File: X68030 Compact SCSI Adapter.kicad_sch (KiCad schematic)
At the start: 2 parts, among them J1 X68030 Internal SCSI Connector, J2 DB25_Plug_MountingHoles

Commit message: Rev 2.0
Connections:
- net ATN: now also J1.35 (Pin_35); no longer J1.32 (Pin_32)
- net CD: now also J1.44 (Pin_44); no longer J1.46 (Pin_46)
- net DB0: now also J1.16 (Pin_16); no longer J1.2 (Pin_2)
- net DB1: now also J1.18 (Pin_18); no longer J1.4 (Pin_4)
- net DB2: now also J1.20 (Pin_20); no longer J1.6 (Pin_6)
- net DB3: now also J1.22 (Pin_22); no longer J1.8 (Pin_8)
- net DB4: now also J1.24 (Pin_24); no longer J1.10 (Pin_10)
- net DB5: now also J1.26 (Pin_26); no longer J1.12 (Pin_12)
- net DB6: now also J1.28 (Pin_28); no longer J1.14 (Pin_14)
- net DB7: now also J1.30 (Pin_30); no longer J1.16 (Pin_16)
- net DBP: now also J1.32 (Pin_32); no longer J1.18 (Pin_18)
- net GND: now also J1.14 (Pin_14), J1.25 (Pin_25), J1.48 (Pin_48); no longer J1.1 (Pin_1), J1.11 (Pin_11), J1.20 (Pin_20), J1.22 (Pin_22), J1.24 (Pin_24), J1.27 (Pin_27), J1.28 (Pin_28), J1.3 (Pin_3), J1.30 (Pin_30), J1.34 (Pin_34), J1.35 (Pin_35), J1.39 (Pin_39), J1.43 (Pin_43), J1.49 (Pin_49), J1.5 (Pin_5), J1.7 (Pin_7), J1.9 (Pin_9)
- net IO: now also J1.43 (Pin_43); no longer J1.50 (Pin_50)
- net MSG: now also J1.40 (Pin_40); no longer J1.42 (Pin_42)
- net REQ: now also J1.46 (Pin_46); no longer J1.48 (Pin_48)
- net RST: now also J1.39 (Pin_39); no longer J1.40 (Pin_40)
- net SEL: now also J1.42 (Pin_42); no longer J1.44 (Pin_44)
- net +5V renamed VCC
- net VCC: now also J1.11 (Pin_11), J1.12 (Pin_12), J1.49 (Pin_49), J1.50 (Pin_50); no longer J1.26 (Pin_26)
- new net HD LED: J1.8 (Pin_8)
- new net ID1: J1.5 (Pin_5)
- new net ID2: J1.6 (Pin_6)
- new net ID4: J1.7 (Pin_7)
- new net TMPWR: J1.34 (Pin_34)
- no-connect marks 1 -> 7

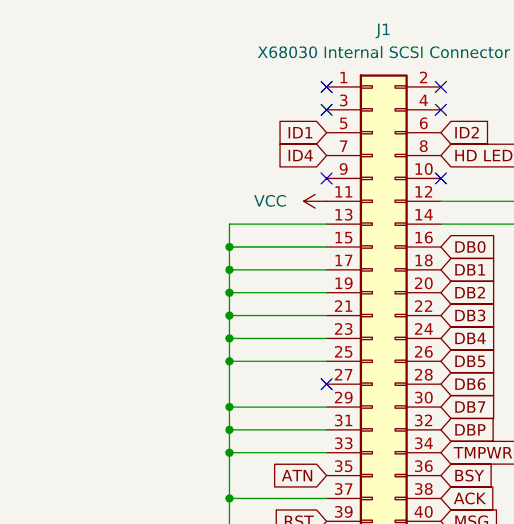
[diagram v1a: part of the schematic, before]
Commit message: Fabricated Rev 2.0 with pinout based on CZ-147 Service Manual for X68030 Compact
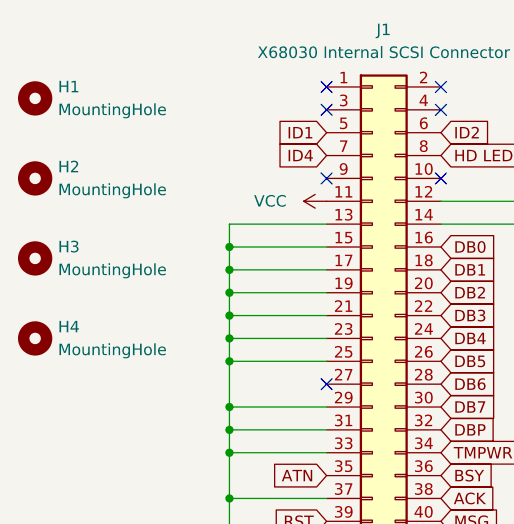
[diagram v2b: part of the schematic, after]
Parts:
- added H1, H2: MountingHole, MountingHole:MountingHole_3.5mm_Pad, symbol Mechanical:MountingHole
- added H3, H4: MountingHole, MountingHole:MountingHole_2.1mm, symbol Mechanical:MountingHole
